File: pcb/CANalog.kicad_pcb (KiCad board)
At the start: 2 copper layers, 100 x 45 mm, 96 parts, among them J1 PWR, J2 USB_B_Micro, J3 SPI3, J4 I2C2, J5 STM_PROG, J6 ESP_PROG, J7 AOUT, J8 CAN, Q1 DMP3099L-7, Q2 MMBT2222A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

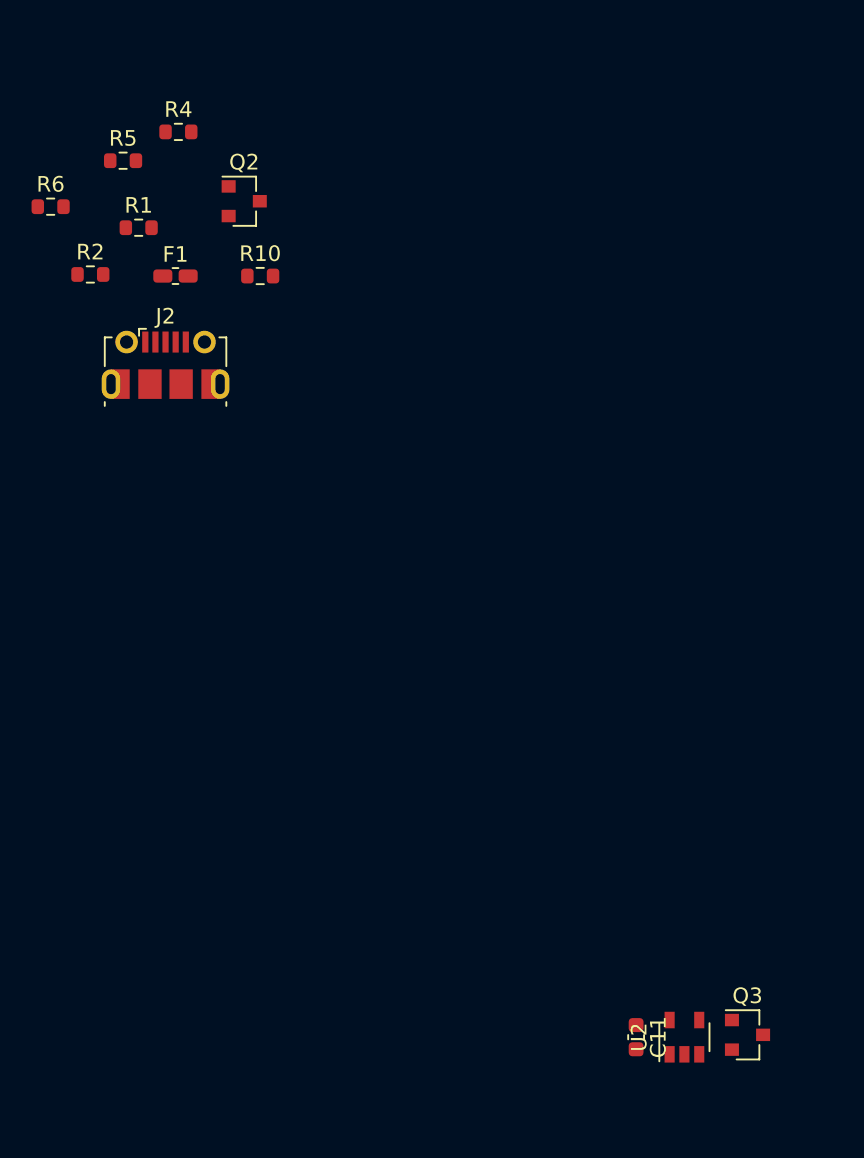
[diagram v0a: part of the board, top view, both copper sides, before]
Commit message: remove usb
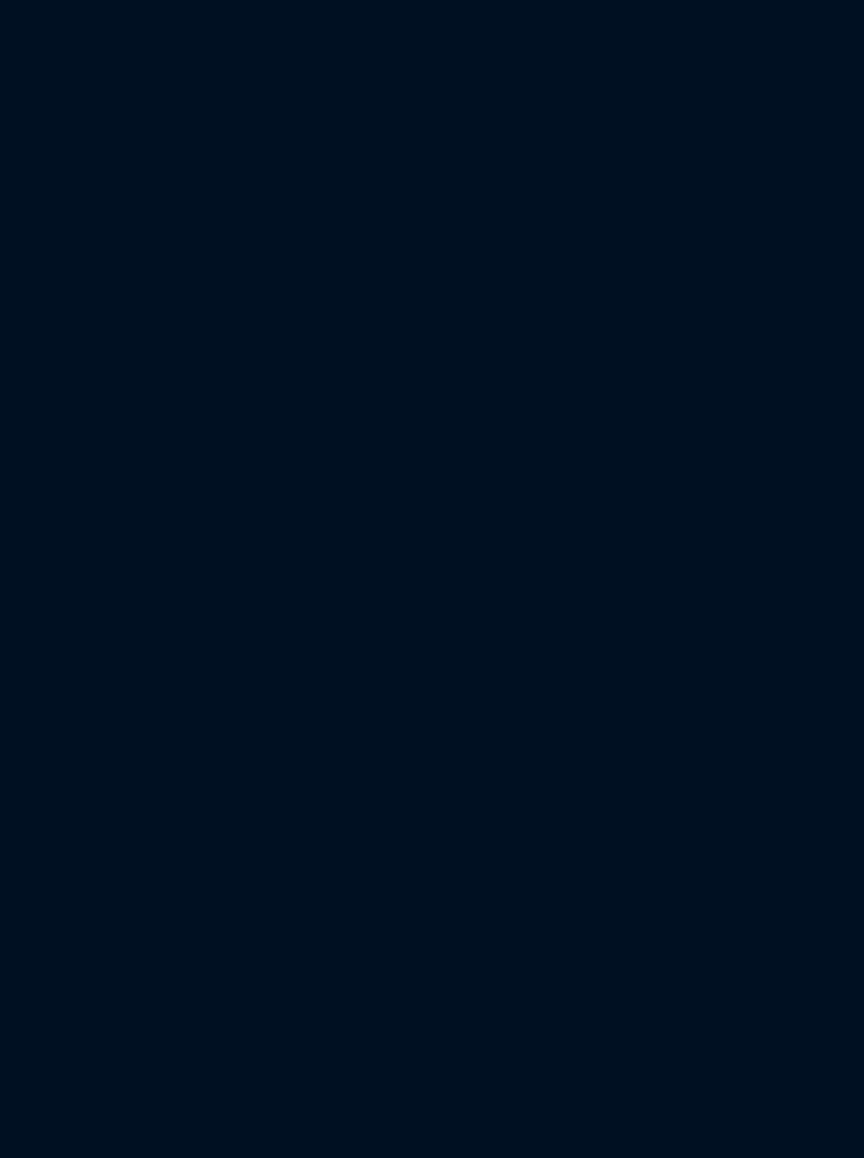
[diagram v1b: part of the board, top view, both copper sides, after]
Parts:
- removed C11: 100nF, Capacitor_SMD:C_0603_1608Metric
- removed F1: 500mA, Fuse:Fuse_0603_1608Metric_Castellated
- removed J2: USB_B_Micro, Connector_USB:USB_Micro-B_Molex-105017-0001
- removed Q2: MMBT2222A, Package_TO_SOT_SMD:SOT-23
- removed Q3: DMP3099L-7, Package_TO_SOT_SMD:SOT-23
- removed R1, R2: 0, Resistor_SMD:R_0603_1608Metric
- removed R10: 1.5k, Resistor_SMD:R_0603_1608Metric
- removed R4: 10k, Resistor_SMD:R_0603_1608Metric
- removed R5, R6: 20k, Resistor_SMD:R_0603_1608Metric
- removed U2: RS321BXF, Package_TO_SOT_SMD:SOT-23-5

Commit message: Update CANalog.kicad_pcb
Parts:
- NT1: moved to B.Cu
- moved J5 126.8 mm to (80.2, 142.3), turned to 270 degrees
- moved U3 105.5 mm to (65.0, 162.4)
- moved NT1 101.2 mm to (63.2, 161.2), turned to 180 degrees
- moved U5 92.2 mm to (50.8, 156.2)
- moved C14 92.1 mm to (47.6, 153.8), turned to 90 degrees
- moved C10 91.1 mm to (94.5, 172.6)
- moved C2 91.1 mm to (89.2, 171.7)
- moved C4 91.1 mm to (91.3, 175.8)
- moved C6 91.1 mm to (90.8, 179.9)
- moved C8 91.1 mm to (86.9, 175.3)
- moved FB1 91.1 mm to (92.8, 167.9)
- moved JP1 89.0 mm to (65.0, 154.8)
- moved C15 86.4 mm to (50.8, 153.1), turned to 180 degrees
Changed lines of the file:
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@@
     (add_net V_B2)
   )
-  (module NetTie:NetTie-2_SMD_Pad0.5mm (layer F.Cu)
-    (at 134.8 89.6)
+  (module NetTie:NetTie-2_SMD_Pad0.5mm (layer B.Cu)
+    (at 63.25 161.2 180)
     (descr "Net tie, 2 pin, 0.5mm square SMD pads")
     (tags "net tie")
     (attr virtual)
-    (fp_text reference NT1 (at 0 -1.2) (layer F.SilkS)
-      (effects (font (size 1 1) (thickness 0.15)))
-    )
-    (fp_text value Net-Tie_2 (at 0 1.2) (layer F.Fab)
-      (effects (font (size 1 1) (thickness 0.15)))
-    )
-    (fp_poly (pts (xy -0.5 -0.25) (xy 0.5 -0.25) (xy 0.5 0.25) (xy -0.5 0.25)) (layer F.Cu) (width 0))
-    (fp_line (start 1 -0.5) (end -1 -0.5) (layer F.CrtYd) (width 0.05))
-    (fp_line (start 1 0.5) (end 1 -0.5) (layer F.CrtYd) (width 0.05))
-    (fp_line (start -1 0.5) (end 1 0.5) (layer F.CrtYd) (width 0.05))
-    (fp_line (start -1 -0.5) (end -1 0.5) (layer F.CrtYd) (width 0.05))
-    (pad 2 smd circle (at 0.5 0) (size 0.5 0.5) (layers F.Cu)
+    (fp_text reference NT1 (at 0 1.2 180) (layer B.SilkS)
+      (effects (font (size 1 1) (thickness 0.15)) (justify mirror))
+    )
+    (fp_text value Net-Tie_2 (at 0 -1.2 180) (layer B.Fab)
+      (effects (font (size 1 1) (thickness 0.15)) (justify mirror))
+    )
+    (fp_poly (pts (xy -0.5 0.25) (xy 0.5 0.25) (xy 0.5 -0.25) (xy -0.5 -0.25)) (layer B.Cu) (width 0))
+    (fp_line (start 1 0.5) (end -1 0.5) (layer B.CrtYd) (width 0.05))
+    (fp_line (start 1 -0.5) (end 1 0.5) (layer B.CrtYd) (width 0.05))
+    (fp_line (start -1 -0.5) (end 1 -0.5) (layer B.CrtYd) (width 0.05))
+    (fp_line (start -1 0.5) (end -1 -0.5) (layer B.CrtYd) (width 0.05))
+    (pad 2 smd circle (at 0.5 0 180) (size 0.5 0.5) (layers B.Cu)
       (net 10 GNDA))
-    (pad 1 smd circle (at -0.5 0) (size 0.5 0.5) (layers F.Cu)
+    (pad 1 smd circle (at -0.5 0 180) (size 0.5 0.5) (layers B.Cu)
       (net 1 GND))
   )
@@
   )
   (module Capacitor_SMD:C_0603_1608Metric (layer F.Cu)
-    (at 83.025 72.9)
+    (at 50.8 153.1 180)
     (descr "Capacitor SMD 0603 (1608 Metric), square (rectangular) end terminal, IPC_7351 nominal, (Body size source: IPC-SM-782 page 76, https://www.pcb-3d.com/wordpress/wp-content/uploads/ipc-sm-782a_amendment_1_and_2.pdf), generated with kicad-footprint-generator")
     (tags capacitor)
@@
       (effects (font (size 0.4 0.4) (thickness 0.06)))
     )
-    (pad 2 smd roundrect (at 0.775 0) (size 0.9 0.95) (layers F.Cu F.Paste F.Mask) (roundrect_rratio 0.25)
-      (net 1 GND))
-    (pad 1 smd roundrect (at -0.775 0) (size 0.9 0.95) (layers F.Cu F.Paste F.Mask) (roundrect_rratio 0.25)
+    (pad 2 smd roundrect (at 0.775 0 180) (size 0.9 0.95) (layers F.Cu F.Paste F.Mask) (roundrect_rratio 0.25)
+      (net 1 GND))
+    (pad 1 smd roundrect (at -0.775 0 180) (size 0.9 0.95) (layers F.Cu F.Paste F.Mask) (roundrect_rratio 0.25)
       (net 6 +3V3))
     (model ${KISYS3DMOD}/Capacitor_SMD.3dshapes/C_0603_1608Metric.wrl
@@
   )
   (module Capacitor_SMD:C_0603_1608Metric (layer F.Cu)
-    (at 82.925 68.75)
+    (at 47.6 153.85 90)
     (descr "Capacitor SMD 0603 (1608 Metric), square (rectangular) end terminal, IPC_7351 nominal, (Body size source: IPC-SM-782 page 76, https://www.pcb-3d.com/wordpress/wp-content/uploads/ipc-sm-782a_amendment_1_and_2.pdf), generated with kicad-footprint-generator")
     (tags capacitor)
     (attr smd)
-    (fp_text reference C14 (at 0 -1.43) (layer F.SilkS)
-      (effects (font (size 1 1) (thickness 0.15)))
-    )
-    (fp_text value 1uF (at 0 1.43) (layer F.Fab)
+    (fp_text reference C14 (at 0 -1.43 90) (layer F.SilkS)
+      (effects (font (size 1 1) (thickness 0.15)))
+    )
+    (fp_text value 1uF (at 0 1.43 90) (layer F.Fab)
       (effects (font (size 1 1) (thickness 0.15)))
     )
@@
     (fp_line (start 1.48 -0.73) (end 1.48 0.73) (layer F.CrtYd) (width 0.05))
     (fp_line (start 1.48 0.73) (end -1.48 0.73) (layer F.CrtYd) (width 0.05))
-    (fp_text user %R (at 0 0) (layer F.Fab)
-      (effects (font (size 0.4 0.4) (thickness 0.06)))
-    )
-    (pad 2 smd roundrect (at 0.775 0) (size 0.9 0.95) (layers F.Cu F.Paste F.Mask) (roundrect_rratio 0.25)
-      (net 1 GND))
-    (pad 1 smd roundrect (at -0.775 0) (size 0.9 0.95) (layers F.Cu F.Paste F.Mask) (roundrect_rratio 0.25)
+    (fp_text user %R (at 0 0 90) (layer F.Fab)
+      (effects (font (size 0.4 0.4) (thickness 0.06)))
+    )
+    (pad 2 smd roundrect (at 0.775 0 90) (size 0.9 0.95) (layers F.Cu F.Paste F.Mask) (roundrect_rratio 0.25)
+      (net 1 GND))
+    (pad 1 smd roundrect (at -0.775 0 90) (size 0.9 0.95) (layers F.Cu F.Paste F.Mask) (roundrect_rratio 0.25)
       (net 12 +5V))
     (model ${KISYS3DMOD}/Capacitor_SMD.3dshapes/C_0603_1608Metric.wrl
@@
   )
   (module Capacitor_SMD:C_0603_1608Metric (layer F.Cu)
-    (at 141.925 94.8)
+    (at 94.475 172.6)
     (descr "Capacitor SMD 0603 (1608 Metric), square (rectangular) end terminal, IPC_7351 nominal, (Body size source: IPC-SM-782 page 76, https://www.pcb-3d.com/wordpress/wp-content/uploads/ipc-sm-782a_amendment_1_and_2.pdf), generated with kicad-footprint-generator")
     (tags capacitor)
@@
   )
   (module Capacitor_SMD:C_0603_1608Metric (layer F.Cu)
-    (at 134.375 97.5)
+    (at 86.925 175.3)
     (descr "Capacitor SMD 0603 (1608 Metric), square (rectangular) end terminal, IPC_7351 nominal, (Body size source: IPC-SM-782 page 76, https://www.pcb-3d.com/wordpress/wp-content/uploads/ipc-sm-782a_amendment_1_and_2.pdf), generated with kicad-footprint-generator")
     (tags capacitor)
@@
   )
   (module Capacitor_SMD:C_0603_1608Metric (layer F.Cu)
-    (at 138.225 102.1)
+    (at 90.775 179.9)
     (descr "Capacitor SMD 0603 (1608 Metric), square (rectangular) end terminal, IPC_7351 nominal, (Body size source: IPC-SM-782 page 76, https://www.pcb-3d.com/wordpress/wp-content/uploads/ipc-sm-782a_amendment_1_and_2.pdf), generated with kicad-footprint-generator")
     (tags capacitor)
@@
   )
   (module Capacitor_SMD:C_0603_1608Metric (layer F.Cu)
-    (at 138.725 98)
+    (at 91.275 175.8)
     (descr "Capacitor SMD 0603 (1608 Metric), square (rectangular) end terminal, IPC_7351 nominal, (Body size source: IPC-SM-782 page 76, https://www.pcb-3d.com/wordpress/wp-content/uploads/ipc-sm-782a_amendment_1_and_2.pdf), generated with kicad-footprint-generator")
     (tags capacitor)
@@
   )
   (module Capacitor_SMD:C_0603_1608Metric (layer F.Cu)
-    (at 136.625 93.85)
+    (at 89.175 171.65)
     (descr "Capacitor SMD 0603 (1608 Metric), square (rectangular) end terminal, IPC_7351 nominal, (Body size source: IPC-SM-782 page 76, https://www.pcb-3d.com/wordpress/wp-content/uploads/ipc-sm-782a_amendment_1_and_2.pdf), generated with kicad-footprint-generator")
     (tags capacitor)
@@
   )
   (module Package_TO_SOT_SMD:SOT-23-5 (layer F.Cu)
-    (at 87.9 71.7)
+    (at 50.8 156.15)
     (descr "5-pin SOT23 package")
     (tags SOT-23-5)
@@
   )
   (module Package_QFP:LQFP-48_7x7mm_P0.5mm (layer F.Cu)
-    (at 150.05 100 315)
+    (at 65 162.45 315)
     (descr "LQFP, 48 Pin (https://www.analog.com/media/en/technical-documentation/data-sheets/ltc2358-16.pdf), generated with kicad-footprint-generator ipc_gullwing_generator.py")
     (tags "LQFP QFP")
@@
   )
   (module Jumper:SolderJumper-2_P1.3mm_Bridged_RoundedPad1.0x1.5mm (layer F.Cu)
-    (at 129.95 93.9)
+    (at 65 154.8)
     (descr "SMD Solder Jumper, 1x1.5mm, rounded Pads, 0.3mm gap, bridged with 1 copper strip")
     (tags "solder jumper open")
@@
   )
   (module Connector_PinHeader_2.54mm:PinHeader_1x04_P2.54mm_Vertical (layer F.Cu)
-    (at 48.15 19.64)
+    (at 80.25 142.3 270)
     (descr "Through hole straight pin header, 1x04, 2.54mm pitch, single row")
     (tags "Through hole pin header THT 1x04 2.54mm single row")
-    (fp_text reference J5 (at 0 -2.33) (layer F.SilkS)
-      (effects (font (size 1 1) (thickness 0.15)))
-    )
-    (fp_text value STM_PROG (at 0 9.95) (layer F.Fab)
+    (fp_text reference J5 (at 0 -2.33 90) (layer F.SilkS)
+      (effects (font (size 1 1) (thickness 0.15)))
+    )
+    (fp_text value STM_PROG (at 0 9.95 90) (layer F.Fab)
       (effects (font (size 1 1) (thickness 0.15)))
     )
@@
     (fp_line (start 1.8 9.4) (end 1.8 -1.8) (layer F.CrtYd) (width 0.05))
     (fp_line (start 1.8 -1.8) (end -1.8 -1.8) (layer F.CrtYd) (width 0.05))
-    (fp_text user %R (at 0 3.81 90) (layer F.Fab)
-      (effects (font (size 1 1) (thickness 0.15)))
-    )
-    (pad 4 thru_hole oval (at 0 7.62) (size 1.7 1.7) (drill 1) (layers *.Cu *.Mask)
-      (net 1 GND))
-    (pad 3 thru_hole oval (at 0 5.08) (size 1.7 1.7) (drill 1) (layers *.Cu *.Mask)
+    (fp_text user %R (at 0 3.81) (layer F.Fab)
+      (effects (font (size 1 1) (thickness 0.15)))
+    )
+    (pad 4 thru_hole oval (at 0 7.62 270) (size 1.7 1.7) (drill 1) (layers *.Cu *.Mask)
+      (net 1 GND))
+    (pad 3 thru_hole oval (at 0 5.08 270) (size 1.7 1.7) (drill 1) (layers *.Cu *.Mask)
       (net 35 /SWCLK))
-    (pad 2 thru_hole oval (at 0 2.54) (size 1.7 1.7) (drill 1) (layers *.Cu *.Mask)
+    (pad 2 thru_hole oval (at 0 2.54 270) (size 1.7 1.7) (drill 1) (layers *.Cu *.Mask)
       (net 36 /SWDIO))
-    (pad 1 thru_hole rect (at 0 0) (size 1.7 1.7) (drill 1) (layers *.Cu *.Mask)
+    (pad 1 thru_hole rect (at 0 0 270) (size 1.7 1.7) (drill 1) (layers *.Cu *.Mask)
       (net 68 "Net-(J5-Pad1)"))
     (model ${KISYS3DMOD}/Connector_PinHeader_2.54mm.3dshapes/PinHeader_1x04_P2.54mm_Vertical.wrl
@@
   )
   (module Inductor_SMD:L_0603_1608Metric (layer F.Cu)
-    (at 140.2875 90.15)
+    (at 92.8375 167.95)
     (descr "Inductor SMD 0603 (1608 Metric), square (rectangular) end terminal, IPC_7351 nominal, (Body size source: http://www.tortai-tech.com/upload/download/2011102023233369053.pdf), generated with kicad-footprint-generator")
     (tags inductor)
